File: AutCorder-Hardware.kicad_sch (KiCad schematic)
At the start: 63 parts, among them J1 Battery, J2 OV2640, J3 EXT LED, J4 Shutter, J5 Util, J6 Feedback, J7 Micro SD, J8 PWR_ALT, P1 USB_C_Plug_USB2.0, Q1 DMP2045U, Q2 DMP2045U, Q3 DMN2040U, SW1 FW, SW2 RESET, U1 ESP32-S3-WROOM-1, U2 MCP73831-2-OT, U3 XC6220B331MR, U4 XC6206P282MR, U5 XC6206P122MR, U6 IMP34DT05TR

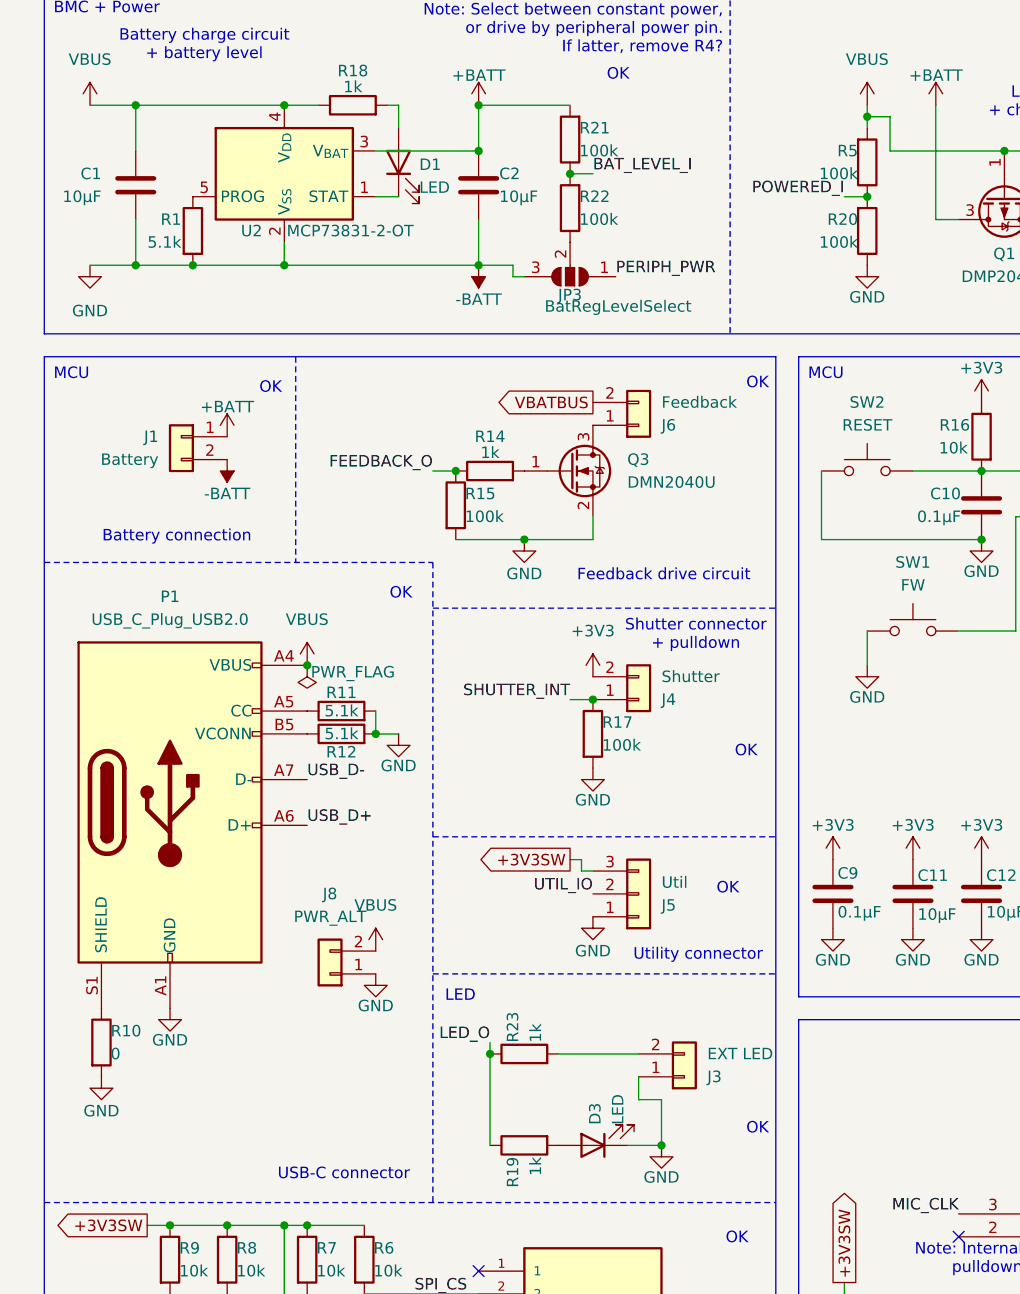
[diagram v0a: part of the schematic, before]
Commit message: Switched R5, Fixed USB data, Removed J3, Removed R10, Reoriented J1, Rearranged components.
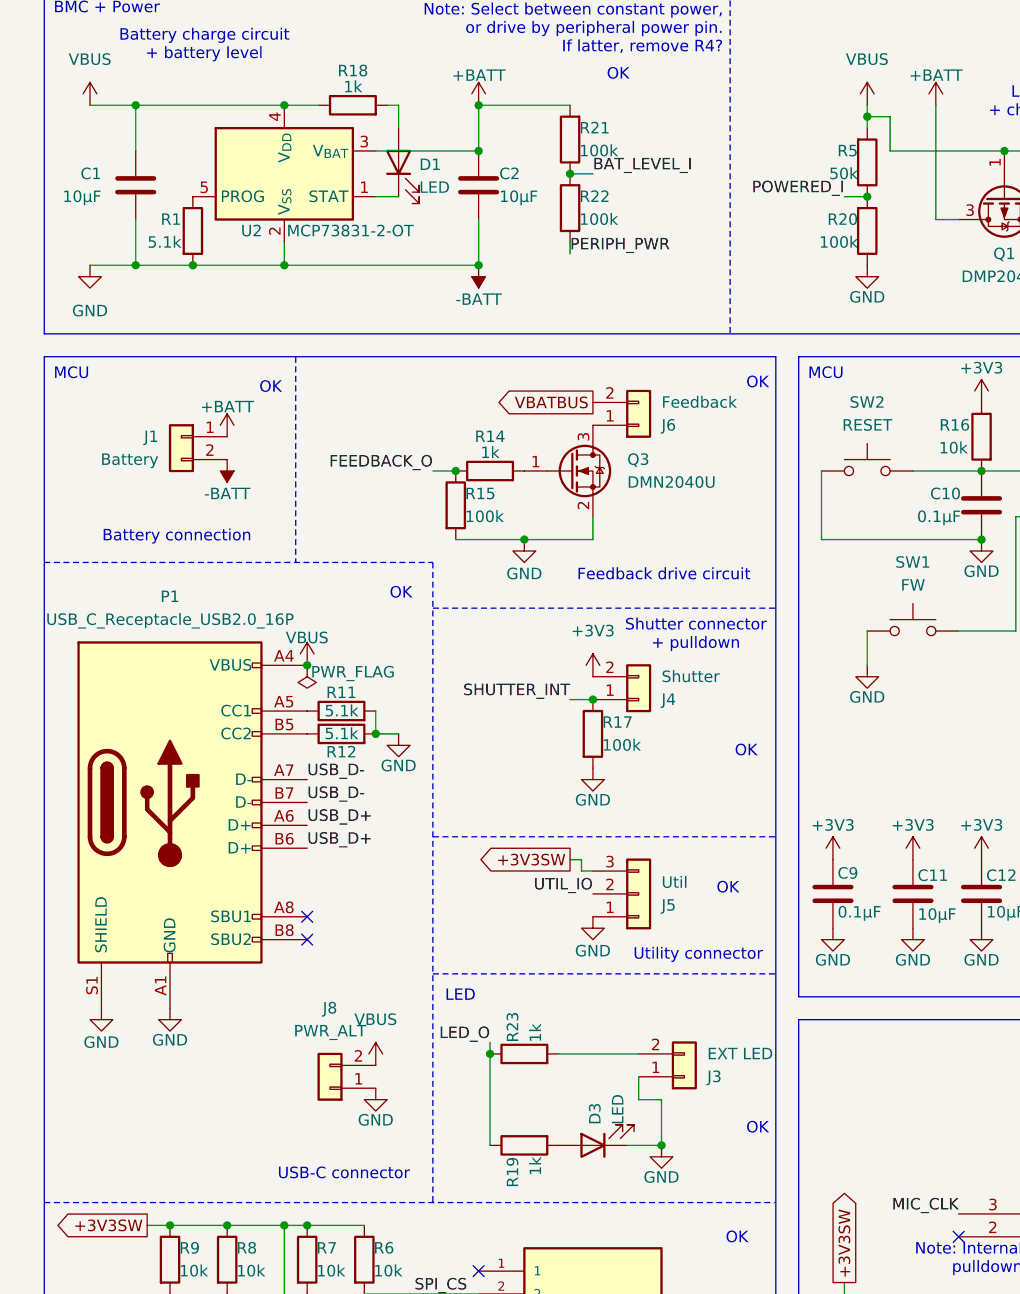
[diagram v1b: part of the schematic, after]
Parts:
- removed JP3: BatRegLevelSelect, 10067099-200LF:SolderJumper-3_P0.75mm_Open_Pad0.5x1mm, symbol Jumper:SolderJumper_3_Open
- removed R10: 0, Resistor_SMD:R_0603_1608Metric, symbol Device:R
- P1: value USB_C_Plug_USB2.0 -> USB_C_Receptacle_USB2.0_16P; symbol Connector:USB_C_Plug_USB2.0 -> Connector:USB_C_Receptacle_USB2.0_16P
- R5: value 100k -> 50k
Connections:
- net -BATT: now also P1.S1 (SHIELD)
- net PERIPH_PWR: now also R22.1
- net USB_D+: now also P1.B6 (D+)
- net USB_D-: now also P1.B7 (D-)
- no-connect marks 12 -> 14
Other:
- moved on the sheet: J8
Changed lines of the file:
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@@
 	)
 	(no_connect
+		(at 44.45 120.65)
+	)
+	(no_connect
 		(at 254 62.23)
 	)
@@
 	)
 	(no_connect
+		(at 44.45 118.11)
+	)
+	(no_connect
 		(at 63.5 175.26)
 	)
@@
 	(wire
 		(pts
-			(xy 67.31 45.72) (xy 63.5 45.72)
+			(xy 73.66 43.18) (xy 73.66 44.45)
 		)
 		(stroke
@@
 		)
 	)
-	(wire
-		(pts
-			(xy 68.58 46.99) (xy 67.31 46.99)
-		)
-		(stroke
-			(width 0)
-			(type default)
-		)
-	)
 	(polyline
 		(pts
@@
 	(wire
 		(pts
-			(xy 67.31 46.99) (xy 67.31 45.72)
-		)
-		(stroke
-			(width 0)
-			(type default)
-		)
-	)
-	(wire
-		(pts
 			(xy 41.91 43.18) (xy 41.91 45.72)
 		)
@@
 		)
 	)
+	(label "USB_D+"
+		(at 44.45 110.49 0)
+		(fields_autoplaced yes)
+		(effects
+			(font
+				(size 1.27 1.27)
+			)
+			(justify left bottom)
+		)
+	)
 	(label "CAM_Y2"
 		(at 246.38 107.95 180)
@@
 	)
 	(label "PERIPH_PWR"
-		(at 78.74 46.99 0)
+		(at 73.66 44.45 0)
 		(fields_autoplaced yes)
 		(effects
@@
 		)
 	)
+	(label "USB_D-"
+		(at 44.45 105.41 0)
+		(fields_autoplaced yes)
+		(effects
+			(font
+				(size 1.27 1.27)
+			)
+			(justify left bottom)
+		)
+	)
 	(label "PERIPH_PWR"
 		(at 213.36 40.64 90)
@@
 	(symbol
 		(lib_id "Connector_Generic:Conn_01x02")
-		(at 46.99 124.46 180)
+		(at 46.99 137.16 180)
 		(unit 1)
 		(exclude_from_sim no)
@@
 		(dnp no)
 		(property "Reference" "J8"
-			(at 46.99 115.57 0)
+			(at 46.99 128.27 0)
 			(effects
 				(font
@@
 		)
 		(property "Value" "PWR_ALT"
-			(at 46.99 118.11 0)
+			(at 46.99 130.81 0)
 			(effects
 				(font
@@
 		)
 		(property "Footprint" "Connector_PinHeader_2.00mm:PinHeader_1x02_P2.00mm_Vertical"
-			(at 46.99 124.46 0)
+			(at 46.99 137.16 0)
 			(effects
 				(font
@@
 		)
 		(property "Datasheet" "~"
-			(at 46.99 124.46 0)
+			(at 46.99 137.16 0)
 			(effects
 				(font
@@
 		)
 		(property "Description" "Generic connector, single row, 01x02, script generated (kicad-library-utils/schlib/autogen/connector/)"
-			(at 46.99 124.46 0)
+			(at 46.99 137.16 0)
 			(effects
 				(font
@@
 	(symbol
 		(lib_id "power:VBUS")
-		(at 52.07 121.92 0)
+		(at 52.07 134.62 0)
 		(unit 1)
 		(exclude_from_sim no)
@@
 		(fields_autoplaced yes)
 		(property "Reference" "#PWR047"
-			(at 52.07 125.73 0)
+			(at 52.07 138.43 0)
 			(effects
 				(font
@@
 		)
 		(property "Value" "VBUS"
-			(at 52.07 116.84 0)
+			(at 52.07 129.54 0)
 			(effects
 				(font
@@
 		)
 		(property "Footprint" ""
-			(at 52.07 121.92 0)
+			(at 52.07 134.62 0)
 			(effects
 				(font
@@
 		)
 		(property "Datasheet" ""
-			(at 52.07 121.92 0)
+			(at 52.07 134.62 0)
 			(effects
 				(font
@@
 		)
 		(property "Description" "Power symbol creates a global label with name \"VBUS\""
-			(at 52.07 121.92 0)
+			(at 52.07 134.62 0)
 			(effects
 				(font
@@
 		(on_board yes)
 		(dnp no)
-		(fields_autoplaced yes)
 		(property "Reference" "#PWR01"
 			(at 44.45 93.98 0)
@@
 		)
 		(property "Value" "VBUS"
-			(at 44.45 85.09 0)
+			(at 44.45 87.122 0)
 			(effects
 				(font
@@
 	)
 	(symbol
-		(lib_id "Connector:USB_C_Plug_USB2.0")
+		(lib_id "Connector:USB_C_Receptacle_USB2.0_16P")
 		(at 29.21 105.41 0)
 		(unit 1)
@@
 			)
 		)
-		(property "Value" "USB_C_Plug_USB2.0"
+		(property "Value" "USB_C_Receptacle_USB2.0_16P"
 			(at 29.21 85.09 0)
 			(effects
@@
 			)
 		)
-		(property "Description" "USB 2.0-only Type-C Plug connector"
+		(property "Description" "USB 2.0-only 16P Type-C Receptacle connector"
 			(at 29.21 105.41 0)
 			(effects
@@
 		(pin "A4"
 		)
+		(pin "A8"
+		)
+		(pin "B7"
+		)
+		(pin "B8"
+		)
+		(pin "B6"
+		)
 		(instances
 			(project "AutCorder-Hardware"
@@
 	(symbol
 		(lib_id "power:GND")
-		(at 21.59 135.89 0)
+		(at 21.59 128.27 0)
 		(unit 1)
 		(exclude_from_sim no)
@@
 		(dnp no)
 		(property "Reference" "#PWR027"
-			(at 21.59 142.24 0)
+			(at 21.59 134.62 0)
 			(effects
 				(font
@@
 		)
 		(property "Value" "GND"
-			(at 21.59 139.7 0)
+			(at 21.59 132.08 0)
 			(effects
 				(font
@@
 		)
 		(property "Footprint" ""
-			(at 21.59 135.89 0)
+			(at 21.59 128.27 0)
 			(effects
 				(font
@@
 		)
 		(property "Datasheet" ""
-			(at 21.59 135.89 0)
+			(at 21.59 128.27 0)
 			(effects
 				(font
@@
 		)
 		(property "Description" "Power symbol creates a global label with name \"GND\" , ground"
-			(at 21.59 135.89 0)
+			(at 21.59 128.27 0)
 			(effects
 				(font
@@
 	)
 	(symbol
-		(lib_id "Device:R")
-		(at 21.59 132.08 0)
-		(unit 1)
-		(exclude_from_sim no)
-		(in_bom yes)
-		(on_board yes)
-		(dnp no)
-		(property "Reference" "R10"
-			(at 22.606 130.81 0)
-			(effects
-				(font
-					(size 1.27 1.27)
-				)
-				(justify left)
-			)
-		)
-		(property "Value" "0"
-			(at 22.606 133.35 0)
-			(effects
-				(font
-					(size 1.27 1.27)
-				)
-				(justify left)
-			)
-		)
-		(property "Footprint" "Resistor_SMD:R_0603_1608Metric"
-			(at 19.812 132.08 90)
-			(effects
-				(font
-					(size 1.27 1.27)
-				)
-				(hide yes)
-			)
-		)
-		(property "Datasheet" "~"
-			(at 21.59 132.08 0)
-			(effects
-				(font
-					(size 1.27 1.27)
-				)
-				(hide yes)
-			)
-		)
-		(property "Description" "Resistor"
-			(at 21.59 132.08 0)
-			(effects
-				(font
-					(size 1.27 1.27)
-				)
-				(hide yes)
-			)
-		)
-		(pin "2"
-		)
-		(pin "1"
-		)
-		(instances
-			(project "AutCorder-Hardware"
-				(path "/f1086080-03e3-4b22-94e1-a270fc7519ac"
-					(reference "R10")
-					(unit 1)
-				)
-			)
-		)
-	)
-	(symbol
 		(lib_id "power:+2V8")
 		(at 254 69.85 90)
@@
 			)
 		)
-		(property "Value" "100k"
+		(property "Value" "50k"
 			(at 105.664 35.56 0)
 			(effects
@@
 	(symbol
 		(lib_id "power:GND")
-		(at 52.07 124.46 0)
+		(at 52.07 137.16 0)
 		(unit 1)
 		(exclude_from_sim no)
@@
 		(dnp no)
 		(property "Reference" "#PWR048"
-			(at 52.07 130.81 0)
+			(at 52.07 143.51 0)
 			(effects
 				(font
@@
 		)
 		(property "Value" "GND"
-			(at 52.07 128.016 0)
+			(at 52.07 140.716 0)
 			(effects
 				(font
@@
 		)
 		(property "Footprint" ""
-			(at 52.07 124.46 0)
+			(at 52.07 137.16 0)
 			(effects
 				(font
@@
 		)
 		(property "Datasheet" ""
-			(at 52.07 124.46 0)
+			(at 52.07 137.16 0)
 			(effects
 				(font
@@
 		)
 		(property "Description" "Power symbol creates a global label with name \"GND\" , ground"
-			(at 52.07 124.46 0)
+			(at 52.07 137.16 0)
 			(effects
 				(font
@@
 					(unit 1)
 				)
-			)
-		)
-	)
-	(symbol
-		(lib_id "Jumper:SolderJumper_3_Open")
-		(at 73.66 46.99 180)
-		(unit 1)
-		(exclude_from_sim yes)
-		(in_bom no)
-		(on_board yes)
-		(dnp no)
-		(property "Reference" "JP3"
-			(at 73.66 49.022 0)
-			(effects
-				(font
-					(size 1.27 1.27)
-				)
-			)
-		)
-		(property "Value" "BatRegLevelSelect"
-			(at 78.994 50.292 0)
-			(effects
-				(font
-					(size 1.27 1.27)
-				)
-			)
-		)
-		(property "Footprint" "10067099-200LF:SolderJumper-3_P0.75mm_Open_Pad0.5x1mm"
-			(at 73.66 46.99 0)
-			(effects
-				(font
-					(size 1.27 1.27)
-				)
-				(hide yes)
-			)
-		)
-		(property "Datasheet" "~"
-			(at 73.66 46.99 0)
-			(effects
-				(font
-					(size 1.27 1.27)
-				)
-				(hide yes)
-			)
-		)
-		(property "Description" "Solder Jumper, 3-pole, open"
-			(at 73.66 46.99 0)
-			(effects
-				(font
-					(size 1.27 1.27)
-				)
-				(hide yes)
-			)
-		)
-		(pin "1"
-		)
-		(pin "3"
-		)
-		(pin "2"
-		)
-		(instances
-			(project "AutCorder-Hardware"
-				(path "/f1086080-03e3-4b22-94e1-a270fc7519ac"
-					(reference "JP3")
-					(unit 1)
-				)

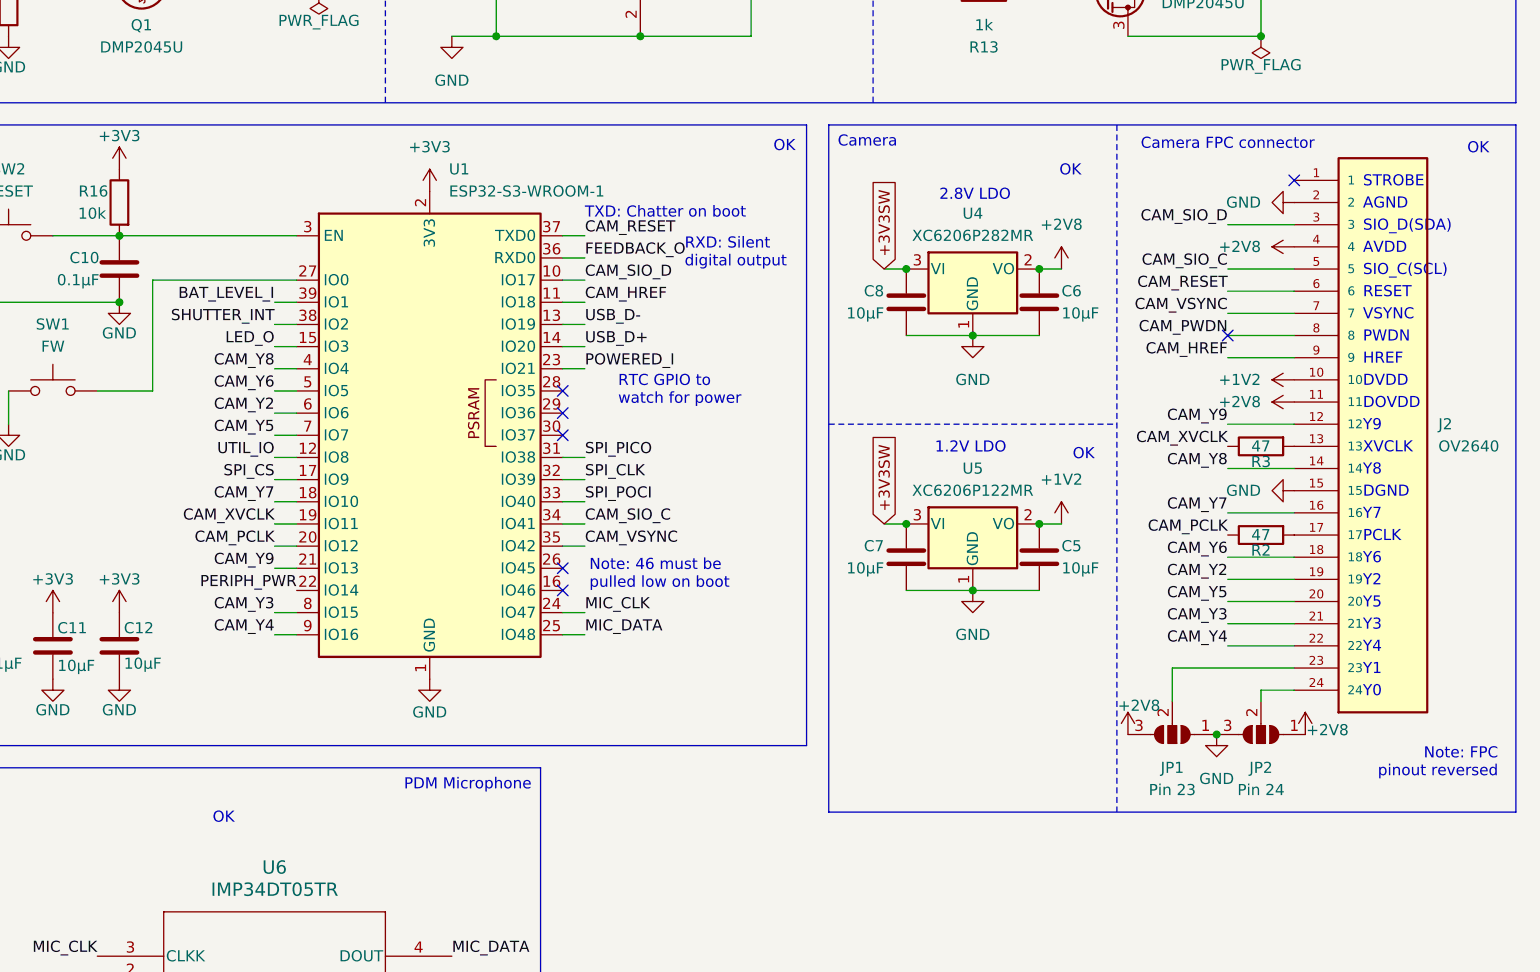
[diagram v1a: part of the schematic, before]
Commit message: Switched to slimmer FPC connector. Rerouted.
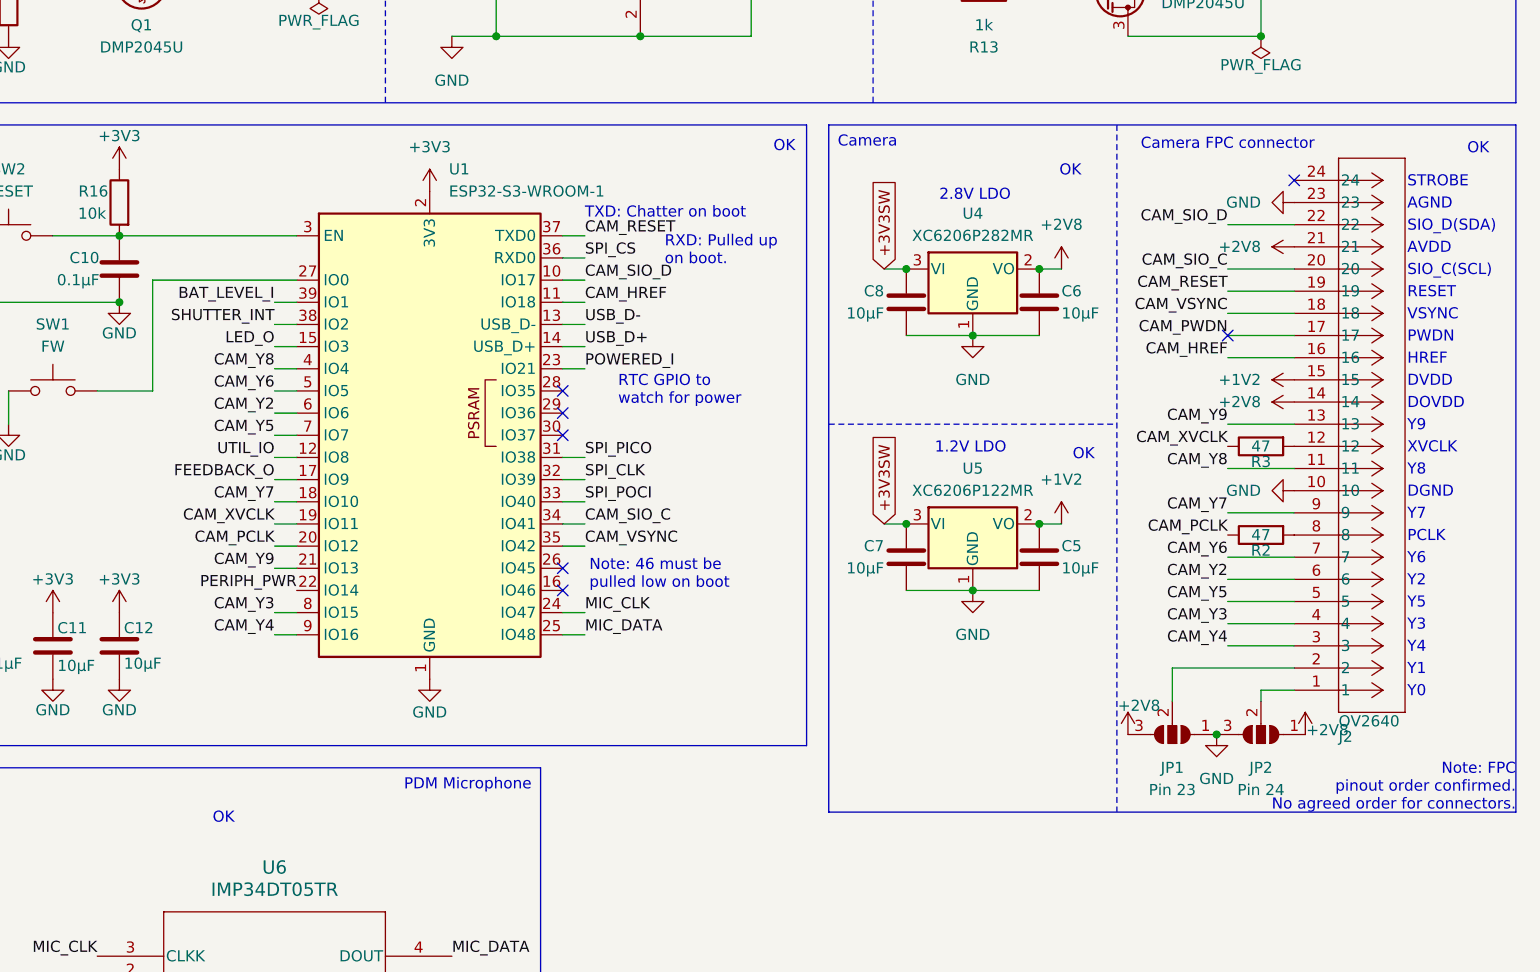
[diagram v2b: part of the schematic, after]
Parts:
- J2: footprint CF35242D0RD-NH:CVILUX_CF35242D0RD-NH -> FFC2B35-24-G:CONN_FFC2B35-24-x_GCT; symbol CF35242D0RD-NH:CF35242D0RD-NH -> FFC2B35-24-G:FFC2B35-24-G
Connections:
- net +1V2: now also J2.15; no longer J2.10
- net +2V8: now also J2.14, J2.21; no longer J2.11, J2.4
- net -BATT: now also J2.10, J2.23; no longer J2.15, J2.2
- net CAM_HREF: now also J2.16; no longer J2.9
- net CAM_PWDN: now also J2.17; no longer J2.8
- net CAM_RESET: now also J2.19; no longer J2.6
- net CAM_SIO_C: now also J2.20; no longer J2.5
- net CAM_SIO_D: now also J2.22; no longer J2.3
- net CAM_VSYNC: now also J2.18; no longer J2.7
- net CAM_Y2: now also J2.6; no longer J2.19
- net CAM_Y3: now also J2.4; no longer J2.21
- net CAM_Y4: now also J2.3; no longer J2.22
- net CAM_Y5: now also J2.5; no longer J2.20
- net CAM_Y6: now also J2.7; no longer J2.18
- net CAM_Y7: now also J2.9; no longer J2.16
- net CAM_Y8: now also J2.11; no longer J2.14
- net CAM_Y9: now also J2.13; no longer J2.12
- net FEEDBACK_O: now also U1.17 (IO9); no longer U1.36 (RXD0)
- net SPI_CS: now also U1.36 (RXD0); no longer U1.17 (IO9)
- net at R2.2: now also J2.8; no longer J2.17
- net at J2.1: now also JP2.2 (C)
- net at R3.2: now also J2.12; no longer J2.13
- net at JP1.2 (C): now also J2.2; no longer J2.23
- net at J2.24: no longer JP2.2 (C)
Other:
- note added: "Note: FPC pinout order confirmed. No agreed order for connectors."
- note added: "RXD: Pulled up on boot."
- note removed: "Note: FPC pinout reversed"
- note removed: "RXD: Silent digital output"
